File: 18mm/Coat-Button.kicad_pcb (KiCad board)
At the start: 2 copper layers, 18 x 18 mm, 27 parts, among them IC1 MADW__ATTINY13-MM, P1 CONN_1, P2 CONN_1, P3 CONN_1, P4 CONN_1

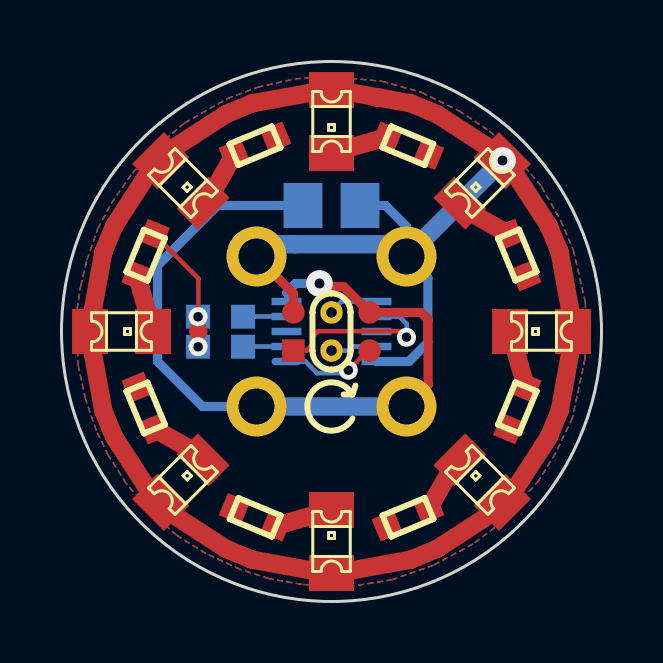
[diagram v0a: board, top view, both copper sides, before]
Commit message: Made one with dual-colour LEDs (0805). Just to see if possible.
Had to use 0402 resitors...
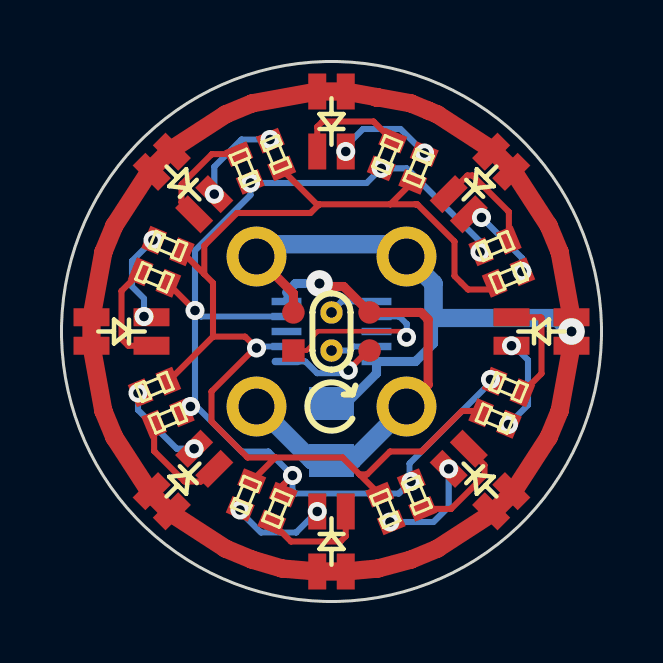
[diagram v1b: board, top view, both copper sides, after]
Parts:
- removed R10, R9: 15, MADW__R0603
- added R1.1: 200, MADW__R0402, F.Cu at (76.8, 56.1)
- added R2.1: 200, MADW__R0402, F.Cu at (80.5, 59.1)
- added R3.1: 200, MADW__R0402, F.Cu at (80.9, 63.9)
- added R4.1: 200, MADW__R0402, F.Cu at (77.8, 67.5)
- added R5.1: 200, MADW__R0402, F.Cu at (73.2, 67.9)
- added R6.1: 200, MADW__R0402, F.Cu at (69.5, 64.9)
- added R7.1: 200, MADW__R0402, F.Cu at (69.1, 60.2)
- added R8.1: 200, MADW__R0402, F.Cu at (72.1, 56.5)
- LED1: renamed from D1; value LED -> MADW__BI-LED; footprint MADW__CHIPLED-0805 -> MADW__CHIPLED-0805-dual
- LED2: renamed from D5; value LED -> MADW__BI-LED; footprint MADW__CHIPLED-0805 -> MADW__CHIPLED-0805-dual
- LED3: renamed from D3; value LED -> MADW__BI-LED; footprint MADW__CHIPLED-0805 -> MADW__CHIPLED-0805-dual
- LED4: renamed from D6; value LED -> MADW__BI-LED; footprint MADW__CHIPLED-0805 -> MADW__CHIPLED-0805-dual
- LED5: renamed from D2; value LED -> MADW__BI-LED; footprint MADW__CHIPLED-0805 -> MADW__CHIPLED-0805-dual
- LED6: renamed from D7; value LED -> MADW__BI-LED; footprint MADW__CHIPLED-0805 -> MADW__CHIPLED-0805-dual
- LED7: renamed from D4; value LED -> MADW__BI-LED; footprint MADW__CHIPLED-0805 -> MADW__CHIPLED-0805-dual
- LED8: renamed from D8; value LED -> MADW__BI-LED; footprint MADW__CHIPLED-0805 -> MADW__CHIPLED-0805-dual
- R1, R2, R3, R4, R5, R6, R7, R8: footprint MADW__R0603 -> MADW__R0402
- moved R5 12.1 mm to (72.2, 67.5), turned to 247.5 degrees
- moved R2 11.6 mm to (80.9, 60.2), turned to 22.5 degrees
- moved R4 11.6 mm to (76.8, 67.9), turned to 292.5 degrees
- moved R6 9.50 mm to (69.1, 63.9), turned to 202.5 degrees
- moved C1 7.55 mm to (75.0, 65.3), turned to 270 degrees
- moved R7 5.45 mm to (69.5, 59.1), turned to 157.5 degrees
- moved R1 0.83 mm to (77.9, 56.5), turned to 67.5 degrees
- moved R3 0.83 mm to (80.5, 64.9), turned to 337.5 degrees
- moved R8 0.76 mm to (73.2, 56.1), turned to 112.5 degrees
- moved G2 0.40 mm to (81.1, 62.0)
- turned LED1 to 90 degrees
- turned LED2 to 45 degrees
- turned LED3 to 0 degrees
- turned LED4 to 315 degrees
- turned LED5 to 270 degrees
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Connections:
- IC1 pad 2: N-0000010 -> /sink_a
- IC1 pad 3: (no net) -> N-0000024
- IC1 pad 4: N-0000011 -> /sink_b
- IC1 pad 8: (no net) -> N-0000026
- LED1 pad 2: N-0000019 -> N-0000013
- LED2 pad 2: N-0000015 -> N-0000014
- LED3 pad 2: N-0000013 -> N-0000015
- LED4 pad 2: N-0000016 -> N-000003
- LED5 pad 2: N-0000020 -> N-000005
- LED6 pad 2: N-0000017 -> N-000007
- LED7 pad 2: N-0000014 -> N-000008
- LED8 pad 2: N-0000018 -> N-0000010
- R1 pad 1: /sink -> /sink_a
- R1 pad 2: N-0000019 -> N-0000021
- R2 pad 1: /sink -> /sink_a
- R2 pad 2: N-0000020 -> N-0000022
- R3 pad 1: /sink -> /sink_a
- R3 pad 2: N-0000013 -> N-000002
- R4 pad 1: /sink -> /sink_a
- R4 pad 2: N-0000014 -> N-000004
- R5 pad 1: /sink -> /sink_a
- R5 pad 2: N-0000015 -> N-000006
- R6 pad 1: /sink -> /sink_a
- R6 pad 2: N-0000016 -> N-000001
- R7 pad 1: /sink -> /sink_a
- R7 pad 2: N-0000017 -> N-000009
- R8 pad 1: /sink -> /sink_a
- R8 pad 2: N-0000018 -> N-0000011
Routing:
- net /sink_a: track 0.00 -> 39.7 mm, vias 0 -> 1
- net /sink_b: track 0.00 -> 36.9 mm, vias 0 -> 8
- net GND: track 26.6 -> 15.3 mm
- net /sink: track 4.92 -> 0.00 mm, vias 2 -> 0
- net N-000003: track 0.00 -> 3.63 mm
- net N-000005: track 0.00 -> 3.63 mm
- net N-000008: track 0.00 -> 3.60 mm
- net N-000007: track 0.00 -> 3.50 mm
- net N-000004: track 0.00 -> 3.48 mm, vias 0 -> 2
- net N-0000021: track 0.00 -> 3.41 mm, vias 0 -> 2
- net N-000009: track 0.00 -> 3.31 mm, vias 0 -> 2
- net N-000006: track 0.00 -> 3.25 mm, vias 0 -> 2
- net N-000002: track 0.00 -> 3.18 mm, vias 0 -> 2
- net N-000001: track 0.00 -> 3.06 mm, vias 0 -> 2
- net N-0000022: track 0.00 -> 2.84 mm, vias 0 -> 2
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- removed copper zone on F.Cu, net /sink
- removed copper zone on B.Cu, net GND
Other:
- net class Default: trace_width 0.1524 -> 0.2032
- board text added: "2013 V0.2.a"
- board text removed: "2013 V0.11.b"
- board text removed: "MCU?"

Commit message: Moved some vias around.
Tracks connecting to them were erroneously deleted by applying
'Delete unconnected tracks'. Now everything is 'solid'.
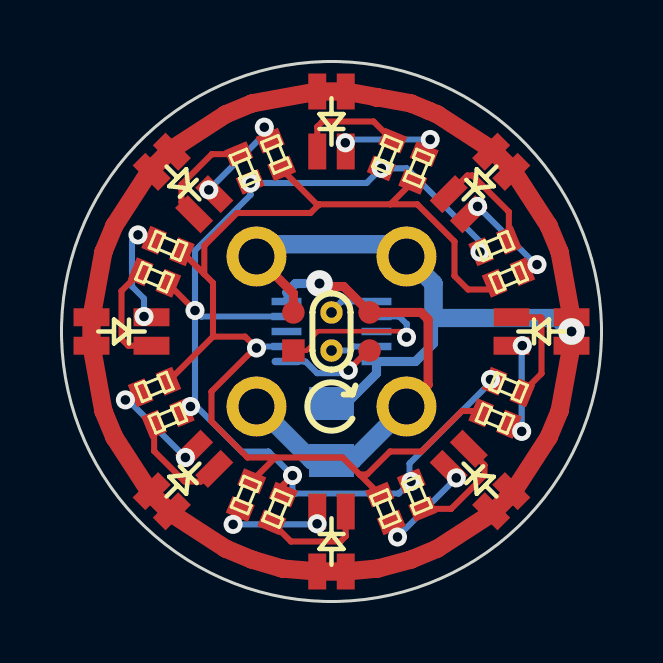
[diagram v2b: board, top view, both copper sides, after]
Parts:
- R1, R1.1, R2, R2.1, R3, R3.1, R4, R4.1, R5, R5.1, R6, R6.1, R7, R7.1, R8, R8.1: value 200 -> 600
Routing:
- net N-0000022: track 2.84 -> 3.77 mm
- net N-000001: track 3.06 -> 3.82 mm
- net N-000006: track 3.25 -> 3.90 mm
- net N-000002: track 3.18 -> 3.76 mm
- net N-000009: track 3.31 -> 3.85 mm

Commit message: Added 2 SOT523 n-ch mosfets + reduced LED resistors.
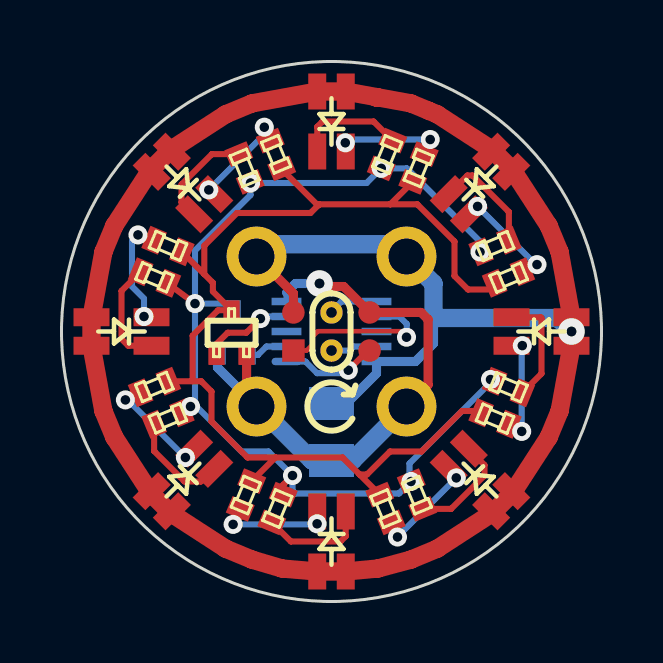
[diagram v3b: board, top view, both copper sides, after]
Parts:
- added Q1: DMG1012T, MADW__SOT523, B.Cu at (71.7, 62.0)
- added Q2: DMG1012T, MADW__SOT523, F.Cu at (71.7, 62.0)
- R1, R1.1, R2, R2.1, R3, R3.1, R4, R4.1, R5, R5.1, R6, R6.1, R7, R7.1, R8, R8.1: value 600 -> 200
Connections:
- IC1 pad 2: /sink_a -> /gate_a
- IC1 pad 4: /sink_b -> /gate_b
- R1 pad 1: /sink_a -> N-0000015
- R1.1 pad 1: /sink_b -> N-000004
- R2 pad 1: /sink_a -> N-0000015
- R2.1 pad 1: /sink_b -> N-000004
- R3 pad 1: /sink_a -> N-0000015
- R3.1 pad 1: /sink_b -> N-000004
- R4 pad 1: /sink_a -> N-0000015
- R4.1 pad 1: /sink_b -> N-000004
- R5 pad 1: /sink_a -> N-0000015
- R5.1 pad 1: /sink_b -> N-000004
- R6 pad 1: /sink_a -> N-0000015
- R6.1 pad 1: /sink_b -> N-000004
- R7 pad 1: /sink_a -> N-0000015
- R7.1 pad 1: /sink_b -> N-000004
- R8 pad 1: /sink_a -> N-0000015
- R8.1 pad 1: /sink_b -> N-000004
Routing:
- net /sink_a: track 39.7 -> 0.00 mm, vias 1 -> 0
- net N-0000015: track 0.00 -> 37.0 mm
- net /sink_b: track 36.9 -> 0.00 mm, vias 8 -> 0
- net N-000004: track 0.00 -> 35.1 mm, vias 0 -> 8
- net GND: track 15.3 -> 19.4 mm
- net /gate_b: track 0.00 -> 3.09 mm, vias 0 -> 1
- net /gate_a: track 0.00 -> 1.42 mm
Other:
- board text added: "2013 V0.21.a"
- board text removed: "2013 V0.2.a"

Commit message: Tweaked some vias.
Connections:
- net N-000001 renamed Net-<LED1-Pad2>
- net N-0000010 renamed Net-<LED7-Pad3>
- net N-0000011 renamed Net-<LED8-Pad2>
- net N-0000012 renamed Net-<LED8-Pad3>
- net N-000002 renamed Net-<R2.1-Pad2>
- net N-0000021 renamed Net-<R1-Pad2>
- net N-0000022 renamed Net-<LED2-Pad3>
- net N-0000023 renamed Net-<R3-Pad2>
- net N-0000024 renamed Net-<R4-Pad2>
- net N-0000025 renamed Net-<R5-Pad2>
- net N-0000026 renamed Net-<IC1-Pad8>
- net N-0000029 renamed Net-<IC1-Pad3>
- net N-000003 renamed Net-<R3.1-Pad2>
- net N-000005 renamed Net-<R4.1-Pad2>
- net N-000006 renamed Net-<R5.1-Pad2>
- net N-000007 renamed Net-<LED6-Pad2>
- net N-000008 renamed Net-<LED6-Pad3>
- net N-000009 renamed Net-<R7.1-Pad2>
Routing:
- net N-000004: track 35.1 -> 36.6 mm
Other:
- board text added: "2013 V0.21.b"
- board text removed: "2013 V0.21.a"

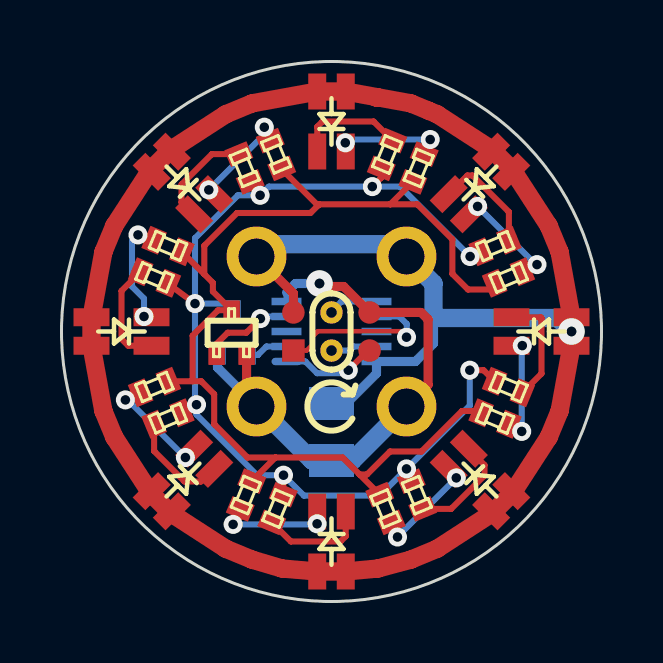
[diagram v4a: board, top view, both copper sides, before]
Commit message: Tweaked SOT523 footprint (backside) for easy drain/source bridging.
Now the same board can be used for single/dual color or just LEDs.
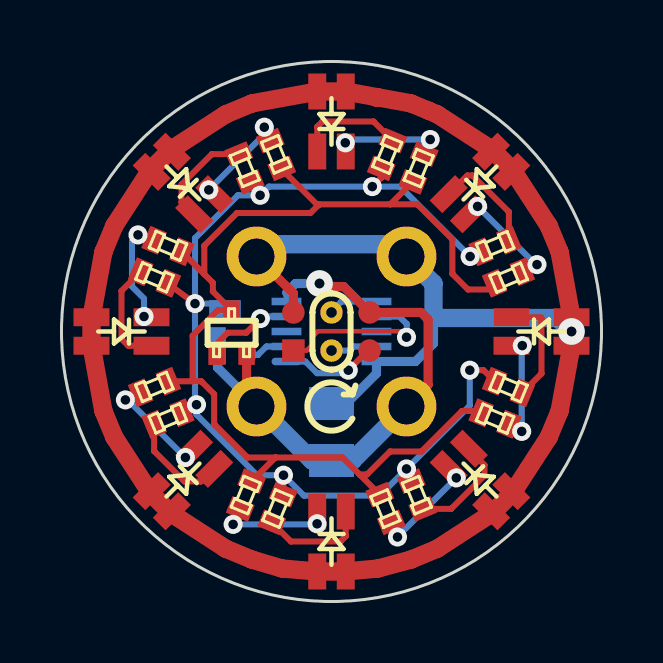
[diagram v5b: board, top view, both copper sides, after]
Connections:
- IC1 pad 3: Net-<IC1-Pad3> -> (no net)
- IC1 pad 8: Net-<IC1-Pad8> -> (no net)
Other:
- board text added: "2013 V0.21.c"
- board text removed: "2013 V0.21.b"

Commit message: Tweaked the BI-LED footprints a bit. Better for normal LEDs.
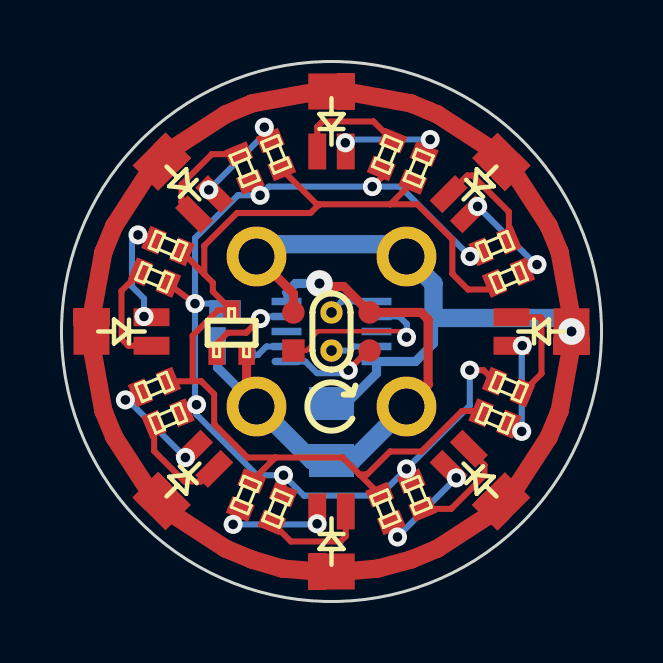
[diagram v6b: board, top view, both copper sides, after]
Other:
- board text added: "2013 V0.21.d"
- board text removed: "2013 V0.21.c"

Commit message: Added alternative 0603 R. footprints for single-color mode.
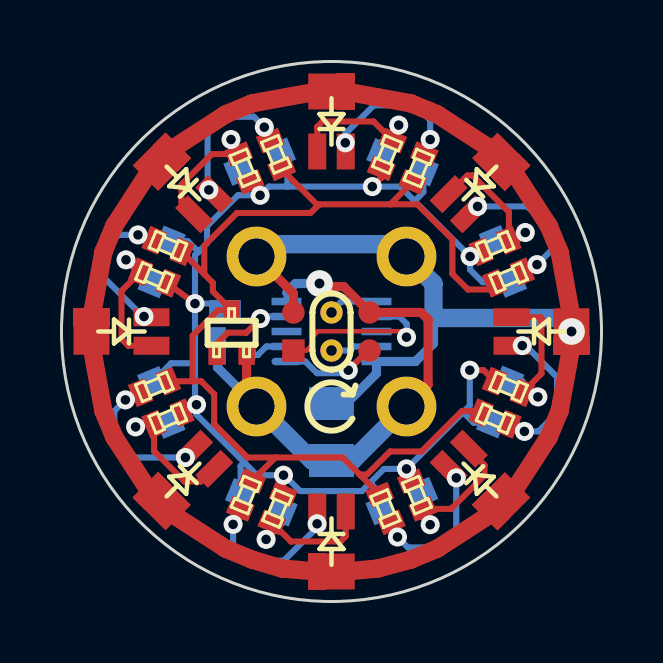
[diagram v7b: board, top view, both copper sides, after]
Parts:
- added R1.2: 200, MADW__R0603, B.Cu at (77.4, 56.4)
- added R2.2: 200, MADW__R0603, B.Cu at (80.7, 59.7)
- added R3.2: 200, MADW__R0603, B.Cu at (80.6, 64.3)
- added R4.2: 200, MADW__R0603, B.Cu at (77.3, 67.7)
- added R5.2: 200, MADW__R0603, B.Cu at (72.7, 67.7)
- added R6.2: 200, MADW__R0603, B.Cu at (69.3, 64.4)
- added R7.2: 200, MADW__R0603, B.Cu at (69.3, 59.7)
- added R8.2: 200, MADW__R0603, B.Cu at (72.6, 56.3)
- moved G2 1.28 mm to (82.4, 62.1)
- moved G1 0.39 mm to (67.6, 61.9)
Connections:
- net N-0000015 renamed Net-<Q2-Pad3>
- net N-000004 renamed Net-<Q1-Pad3>
- net Net-<R1-Pad2> renamed Net-<LED1-Pad3>
- net Net-<R2.1-Pad2> renamed Net-<LED2-Pad2>
- net Net-<R3-Pad2> renamed Net-<LED3-Pad3>
- net Net-<R3.1-Pad2> renamed Net-<LED3-Pad2>
- net Net-<R4-Pad2> renamed Net-<LED4-Pad3>
- net Net-<R4.1-Pad2> renamed Net-<LED4-Pad2>
- net Net-<R5-Pad2> renamed Net-<LED5-Pad3>
- net Net-<R5.1-Pad2> renamed Net-<LED5-Pad2>
- net Net-<R7.1-Pad2> renamed Net-<LED7-Pad2>
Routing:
- net Net-<Q1-Pad3>: track 36.6 -> 46.9 mm
- net Net-<LED7-Pad2>: track 3.60 -> 5.77 mm, vias 0 -> 1
- net Net-<LED3-Pad2>: track 3.77 -> 5.71 mm, vias 0 -> 1
- net Net-<LED6-Pad2>: track 3.50 -> 5.39 mm, vias 0 -> 1
- net Net-<LED2-Pad2>: track 3.71 -> 5.53 mm, vias 0 -> 1
- net Net-<LED5-Pad2>: track 3.63 -> 5.45 mm, vias 0 -> 1
- net Net-<LED4-Pad2>: track 3.63 -> 5.44 mm, vias 0 -> 1
- net Net-<LED1-Pad2>: track 3.68 -> 5.46 mm, vias 0 -> 1
- net Net-<LED8-Pad2>: track 3.51 -> 5.24 mm, vias 0 -> 1
- net Net-<LED5-Pad3>: track 3.90 -> 5.48 mm
- net Net-<LED1-Pad3>: track 3.74 -> 5.24 mm
- net Net-<LED2-Pad3>: track 3.77 -> 5.15 mm
- net Net-<LED4-Pad3>: track 3.79 -> 5.16 mm
- net Net-<LED3-Pad3>: track 3.76 -> 5.11 mm
- net Net-<LED6-Pad3>: track 3.82 -> 5.17 mm
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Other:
- board text added: "0.22.a"
- board text added: "2013"
- board text added: "spitzenpfeil.org"
- board text removed: "2013 V0.21.d"
- board text removed: "blog. spitzenpfeil.org"
